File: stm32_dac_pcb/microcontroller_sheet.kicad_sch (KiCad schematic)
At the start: 2 parts, among them J201 Conn_01x03, U101 STM32F411CEUx

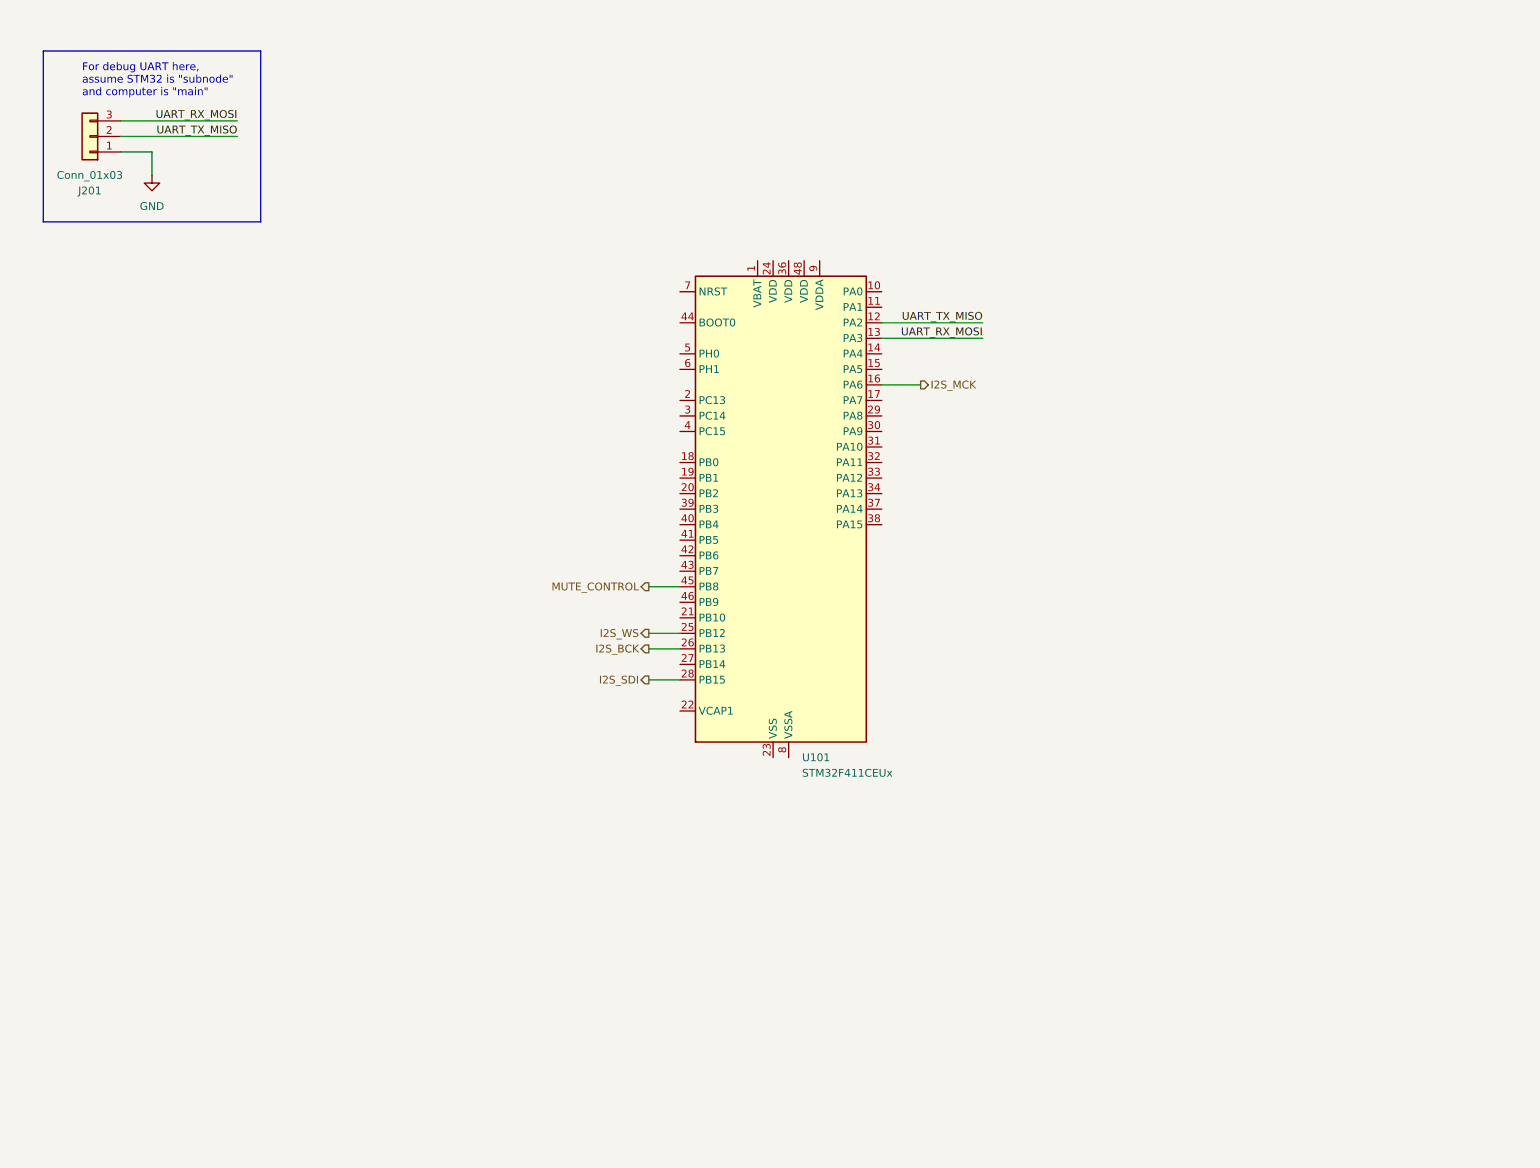
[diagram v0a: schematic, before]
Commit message: Add missing TODOs and USB plug
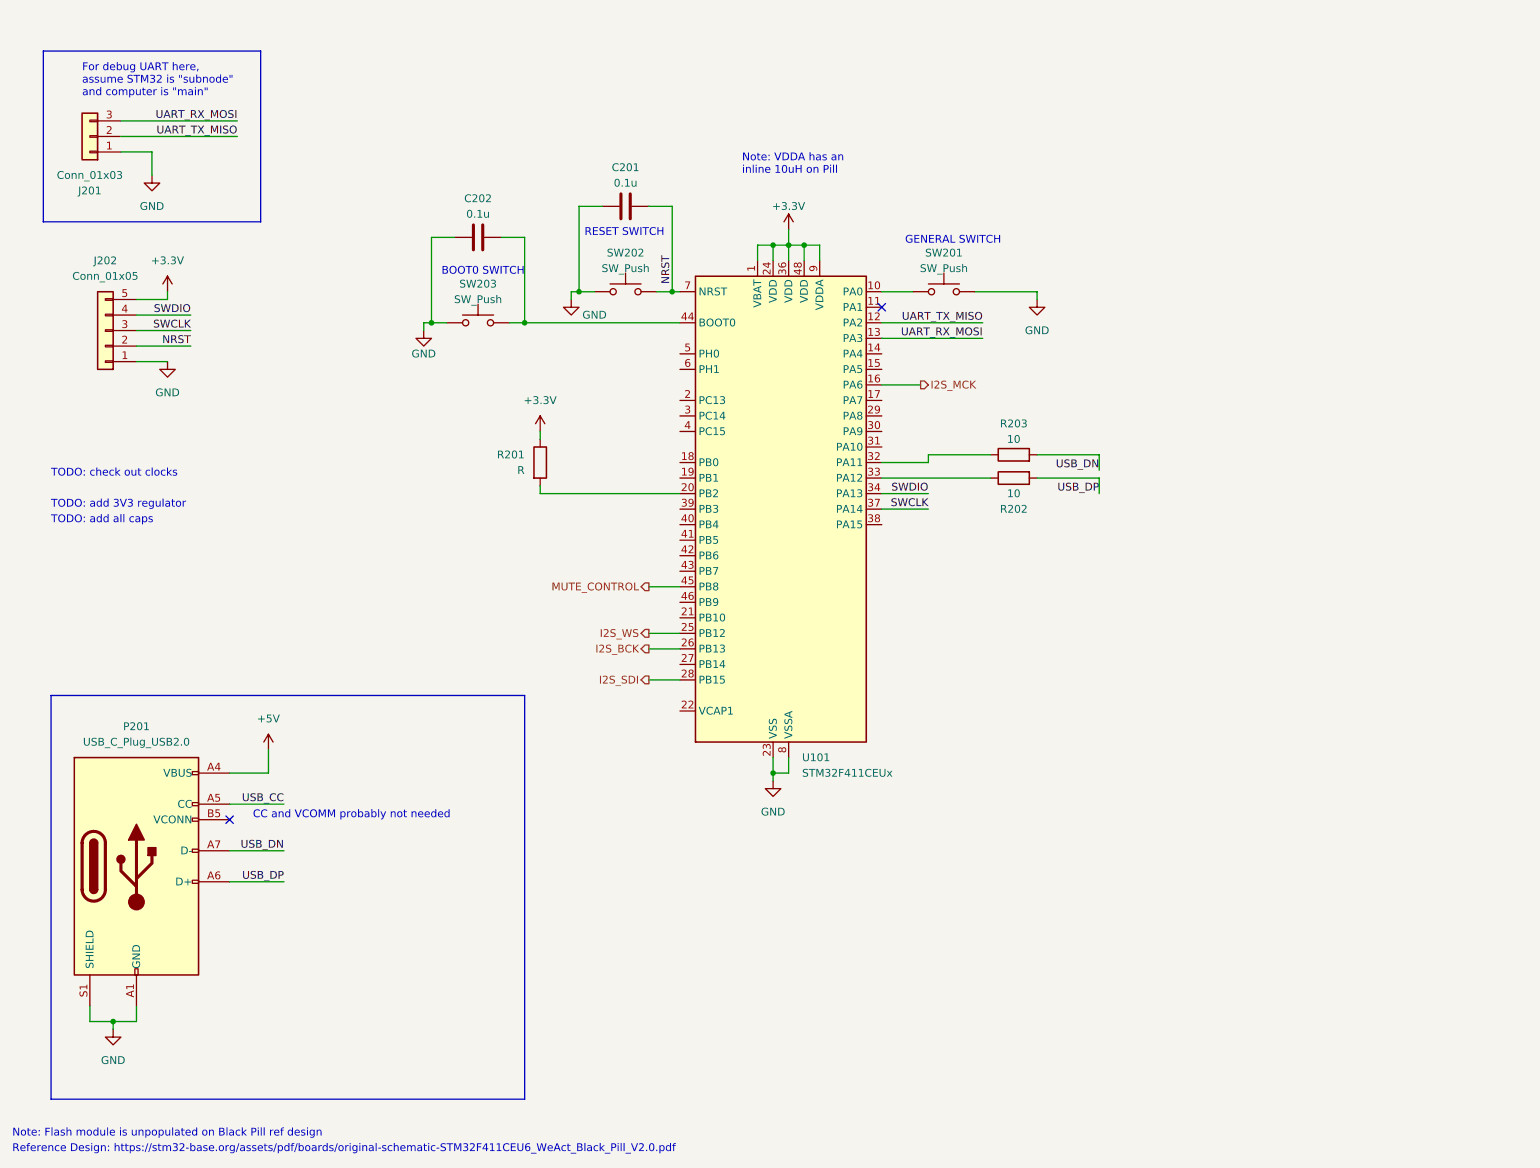
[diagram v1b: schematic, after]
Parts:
- added C201, C202: 0.1u, symbol Device:C
- added J202: Conn_01x05, symbol Connector_Generic:Conn_01x05
- added P201: USB_C_Plug_USB2.0, symbol Connector:USB_C_Plug_USB2.0
- added R201: R, symbol Device:R
- added R202, R203: 10, symbol Device:R
- added SW201, SW202, SW203: SW_Push, symbol Switch:SW_Push
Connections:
- net GND: now also U101.23 (VSS), U101.35 (VSS), U101.47 (VSS), U101.49 (VSS), U101.8 (VSSA), C201.1, C202.1, J202.1 (Pin_1), P201.A1 (GND), P201.A12 (GND), P201.B1 (GND), P201.B12 (GND), P201.S1 (SHIELD), SW201.2, SW202.2, SW203.2
- net +3.3V: now reaches U101.1 (VBAT)
- net +3.3V: now also U101.24 (VDD), U101.36 (VDD), U101.48 (VDD), U101.9 (VDDA), J202.5 (Pin_5), R201.1
- net at U101.10 (PA0): now also SW201.1
- net at U101.20 (PB2): now also R201.2
- net at U101.32 (PA11): now also R203.1
- net at U101.33 (PA12): now also R202.1
- net SWDIO: now reaches U101.34 (PA13)
- net SWDIO: now also J202.4 (Pin_4)
- net SWCLK: now reaches U101.37 (PA14)
- net SWCLK: now also J202.3 (Pin_3)
- net at U101.44 (BOOT0): now also C202.2, SW203.1
- net NRST: now reaches U101.7 (NRST)
- net NRST: now also C201.2, J202.2 (Pin_2), SW202.1
- new net +5V: P201.A4 (VBUS), P201.A9 (VBUS), P201.B4 (VBUS), P201.B9 (VBUS)
- new net USB_CC: P201.A5 (CC)
- new net USB_DN: P201.A7 (D-), R203.2
- new net USB_DP: P201.A6 (D+), R202.2
- no-connect marks 0 -> 2
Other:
- note added: "BOOT0 SWITCH"
- note added: "CC and VCOMM probably not needed"
- note added: "GENERAL SWITCH"
- note added: "Note: Flash module is unpopulated on Black Pill ref design"
- note added: "Note: VDDA has an inline 10uH on Pill"
- note added: "RESET SWITCH"
- note added: "Reference Design: https://stm32-base.org/assets/pdf/boards/original-schematic-STM32F411CEU6_WeAct_Black_Pill_V2.0.pdf"
- note added: "TODO: add 3V3 regulator"
- note added: "TODO: add all caps"
- note added: "TODO: check out clocks"

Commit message: Layout and routing
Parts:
- added C307 (x4): 0.1u, Capacitor_SMD:C_0603_1608Metric_Pad1.08x0.95mm_HandSolder, symbol Device:C
- C201, C202: footprint (none) -> Capacitor_SMD:C_0603_1608Metric_Pad1.08x0.95mm_HandSolder
- J201: footprint (none) -> Connector_PinHeader_2.00mm:PinHeader_1x03_P2.00mm_Vertical
- J202: footprint (none) -> Connector_PinHeader_2.00mm:PinHeader_1x05_P2.00mm_Vertical
- P201: footprint (none) -> Connector_USB:USB_C_Receptacle_CNCTech_C-ARA1-AK51X; LCSC (none) -> C2686966
- R201: value R -> 10k; footprint (none) -> Resistor_SMD:R_0603_1608Metric_Pad0.98x0.95mm_HandSolder
- R202, R203: footprint (none) -> Resistor_SMD:R_0603_1608Metric_Pad0.98x0.95mm_HandSolder
- SW201, SW202, SW203: footprint (none) -> 0_project_fp_lib:PushButtonSMD_2.93x3.9; LCSC (none) -> C18077675
- U101: LCSC (none) -> C60420
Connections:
- net +3.3V: now also C307.1, C307.1, C307.1, C307.1
- net GND: now also C307.2, C307.2, C307.2, C307.2
- net MIC_IN_2: now reaches U101.17 (PA7)
- net I2S_MCK renamed MIC_IN_1
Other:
- note added: "Decoupling for MCU"
- note added: "Note: I2S_MCLK used to be on PA6"
- note added: "Programming Header"
- note added: "TODO: LEDs"
- note added: "USB: LCSC C2686966 G-Switch GT-USB-7029DB"
- note removed: "TODO: add 3V3 regulator"
- note removed: "TODO: add all caps"

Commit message: Mostly finish up
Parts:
- added C307: 2.2u, Capacitor_SMD:C_0603_1608Metric_Pad1.08x0.95mm_HandSolder, symbol Device:C
- added J203: Conn_01x01, Connector_PinHeader_2.00mm:PinHeader_1x01_P2.00mm_Vertical, symbol Connector_Generic:Conn_01x01
- added R204: 5.1k, Resistor_SMD:R_0603_1608Metric_Pad0.98x0.95mm_HandSolder, symbol Device:R
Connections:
- net GND: now also C307.2, R204.2
- net at U101.22 (VCAP1): now also C307.1
- net at P201.B5 (VCONN): now also J203.1 (Pin_1)
- net USB_CC: no longer names the net of P201.A5 (CC)
- net USB_CC: now also R204.1
- no-connect marks 2 -> 22
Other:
- note added: "VCONN probably not needed"
- note removed: "CC and VCOMM probably not needed"
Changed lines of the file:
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@@
   (junction (at 220.98 33.02) (diameter 0) (color 0 0 0 0)
   )
-  (no_connect (at 49.53 147.32))
+  (no_connect (at 156.21 81.28))
+  (no_connect (at 123.19 101.6))
+  (no_connect (at 123.19 88.9))
+  (no_connect (at 123.19 106.68))
+  (no_connect (at 156.21 71.12))
+  (no_connect (at 123.19 99.06))
+  (no_connect (at 123.19 111.76))
+  (no_connect (at 123.19 83.82))
+  (no_connect (at 123.19 114.3))
+  (no_connect (at 123.19 73.66))
+  (no_connect (at 156.21 86.36))
+  (no_connect (at 123.19 78.74))
+  (no_connect (at 123.19 91.44))
+  (no_connect (at 156.21 73.66))
+  (no_connect (at 123.19 121.92))
+  (no_connect (at 156.21 99.06))
+  (no_connect (at 123.19 104.14))
   (no_connect (at 156.21 63.5))
+  (no_connect (at 156.21 83.82))
+  (no_connect (at 123.19 81.28))
+  (no_connect (at 123.19 96.52))
+  (no_connect (at 123.19 71.12))
   (wire (pts (xy 143.51 53.34) (xy 140.97 53.34))
     (stroke (width 0) (type default))
@@
     (stroke (width 0) (type default))
   )
+  (wire (pts (xy 49.53 147.32) (xy 63.5 147.32))
+    (stroke (width 0) (type default))
+  )
   (wire (pts (xy 171.45 60.96) (xy 181.61 60.96))
     (stroke (width 0) (type default))
   )
-  (wire (pts (xy 49.53 144.78) (xy 58.42 144.78))
+  (wire (pts (xy 49.53 144.78) (xy 68.58 144.78))
     (stroke (width 0) (type default))
   )
@@
     (stroke (width 0) (type default))
   )
+  (wire (pts (xy 119.38 139.7) (xy 119.38 142.24))
+    (stroke (width 0) (type default))
+  )
   (wire (pts (xy 121.92 60.96) (xy 123.19 60.96))
     (stroke (width 0) (type default))
@@
     (stroke (width 0) (type default))
   )
+  (wire (pts (xy 119.38 129.54) (xy 123.19 129.54))
+    (stroke (width 0) (type default))
+  )
   (wire (pts (xy 242.57 33.02) (xy 256.54 33.02))
     (stroke (width 0) (type default))
@@
     (stroke (width 0) (type default))
   )
+  (wire (pts (xy 63.5 147.32) (xy 63.5 166.37))
+    (stroke (width 0) (type default))
+  )
   (wire (pts (xy 156.21 96.52) (xy 163.83 96.52))
     (stroke (width 0) (type default))
@@
     (stroke (width 0) (type default))
   )
+  (wire (pts (xy 63.5 166.37) (xy 64.77 166.37))
+    (stroke (width 0) (type default))
+  )
   (wire (pts (xy 215.9 33.02) (xy 220.98 33.02))
     (stroke (width 0) (type default))
@@
     (stroke (width 0) (type default))
   )
+  (wire (pts (xy 119.38 132.08) (xy 119.38 129.54))
+    (stroke (width 0) (type default))
+  )
   (wire (pts (xy 156.21 76.2) (xy 162.56 76.2))
     (stroke (width 0) (type default))
@@
     (stroke (width 0) (type default))
   )
+  (wire (pts (xy 68.58 153.67) (xy 68.58 156.21))
+    (stroke (width 0) (type default))
+  )
   (wire (pts (xy 191.77 87.63) (xy 191.77 90.17))
+    (stroke (width 0) (type default))
+  )
+  (wire (pts (xy 68.58 146.05) (xy 68.58 144.78))
     (stroke (width 0) (type default))
   )
@@
     (effects (font (size 1.27 1.27)) (justify left bottom))
   )
-  (text "CC and VCOMM probably not needed" (at 53.34 147.32 0)
+  (text "VCONN probably not needed" (at 59.69 171.45 0)
     (effects (font (size 1.27 1.27)) (justify left bottom))
   )
@@
   )
   (label "SWCLK" (at 163.83 96.52 180) (fields_autoplaced)
-    (effects (font (size 1.27 1.27)) (justify right bottom))
-  )
-  (label "USB_CC" (at 58.42 144.78 180) (fields_autoplaced)
     (effects (font (size 1.27 1.27)) (justify right bottom))
   )
@@
     )
   )
+  (symbol (lib_id "power:GND") (at 119.38 142.24 0) (unit 1)
+    (in_bom yes) (on_board yes) (dnp no)
+    (property "Reference" "#PWR0214" (at 119.38 148.59 0)
+      (effects (font (size 1.27 1.27)) hide)
+    )
+    (property "Value" "GND" (at 119.38 146.05 0)
+      (effects (font (size 1.27 1.27)))
+    )
+    (property "Footprint" "" (at 119.38 142.24 0)
+      (effects (font (size 1.27 1.27)) hide)
+    )
+    (property "Datasheet" "" (at 119.38 142.24 0)
+      (effects (font (size 1.27 1.27)) hide)
+    )
+    (pin "1")
+    (instances
+      (project "stm32_dac_pcb"
+        (path "/c2a919d7-4260-41a9-9bc5-9737c1b4d769/b77d31d3-d267-4ae4-806f-e210a5dd1f2c"
+          (reference "#PWR0214") (unit 1)
+        )
+      )
+    )
+  )
+  (symbol (lib_id "power:GND") (at 68.58 156.21 0) (unit 1)
+    (in_bom yes) (on_board yes) (dnp no)
+    (property "Reference" "#PWR0215" (at 68.58 162.56 0)
+      (effects (font (size 1.27 1.27)) hide)
+    )
+    (property "Value" "GND" (at 68.58 160.02 0)
+      (effects (font (size 1.27 1.27)))
+    )
+    (property "Footprint" "" (at 68.58 156.21 0)
+      (effects (font (size 1.27 1.27)) hide)
+    )
+    (property "Datasheet" "" (at 68.58 156.21 0)
+      (effects (font (size 1.27 1.27)) hide)
+    )
+    (pin "1")
+    (instances
+      (project "stm32_dac_pcb"
+        (path "/c2a919d7-4260-41a9-9bc5-9737c1b4d769/b77d31d3-d267-4ae4-806f-e210a5dd1f2c"
+          (reference "#PWR0215") (unit 1)
+        )
+      )
+    )
+  )
   (symbol (lib_id "Device:C") (at 114.3 46.99 90) (unit 1)
     (in_bom yes) (on_board yes) (dnp no)
@@
         (path "/c2a919d7-4260-41a9-9bc5-9737c1b4d769/b77d31d3-d267-4ae4-806f-e210a5dd1f2c"
           (reference "#PWR0201") (unit 1)
+        )
+      )
+    )
+  )
+  (symbol (lib_id "Device:C") (at 119.38 135.89 0) (mirror y) (unit 1)
+    (in_bom yes) (on_board yes) (dnp no)
+    (property "Reference" "C307" (at 116.84 134.62 0)
+      (effects (font (size 1.27 1.27)) (justify left))
+    )
+    (property "Value" "2.2u" (at 116.84 137.16 0)
+      (effects (font (size 1.27 1.27)) (justify left))
+    )
+    (property "Footprint" "Capacitor_SMD:C_0603_1608Metric_Pad1.08x0.95mm_HandSolder" (at 118.4148 139.7 0)
+      (effects (font (size 1.27 1.27)) hide)
+    )
+    (property "Datasheet" "~" (at 119.38 135.89 0)
+      (effects (font (size 1.27 1.27)) hide)
+    )
+    (pin "1")
+    (pin "2")
+    (instances
+      (project "stm32_dac_pcb"
+        (path "/c2a919d7-4260-41a9-9bc5-9737c1b4d769/0d9874eb-1d6a-4e96-92eb-7b248f8c9096"
+          (reference "C307") (unit 1)
+        )
+        (path "/c2a919d7-4260-41a9-9bc5-9737c1b4d769/b77d31d3-d267-4ae4-806f-e210a5dd1f2c"
+          (reference "C207") (unit 1)
+        )
+      )
+    )
+  )
+  (symbol (lib_id "Connector_Generic:Conn_01x01") (at 69.85 166.37 0) (unit 1)
+    (in_bom yes) (on_board yes) (dnp no) (fields_autoplaced)
+    (property "Reference" "J203" (at 72.39 165.1 0)
+      (effects (font (size 1.27 1.27)) (justify left))
+    )
+    (property "Value" "Conn_01x01" (at 72.39 167.64 0)
+      (effects (font (size 1.27 1.27)) (justify left))
+    )
+    (property "Footprint" "Connector_PinHeader_2.00mm:PinHeader_1x01_P2.00mm_Vertical" (at 69.85 166.37 0)
+      (effects (font (size 1.27 1.27)) hide)
+    )
+    (property "Datasheet" "~" (at 69.85 166.37 0)
+      (effects (font (size 1.27 1.27)) hide)
+    )
+    (pin "1")
+    (instances
+      (project "stm32_dac_pcb"
+        (path "/c2a919d7-4260-41a9-9bc5-9737c1b4d769/b77d31d3-d267-4ae4-806f-e210a5dd1f2c"
+          (reference "J203") (unit 1)
         )
       )
@@
         )
       )
+    )
+  )
+  (symbol (lib_id "Device:R") (at 68.58 149.86 0) (mirror y) (unit 1)
+    (in_bom yes) (on_board yes) (dnp no)
+    (property "Reference" "R204" (at 71.12 148.59 0)
+      (effects (font (size 1.27 1.27)) (justify right))
+    )
+    (property "Value" "5.1k" (at 71.12 151.13 0)
+      (effects (font (size 1.27 1.27)) (justify right))
+    )
+    (property "Footprint" "Resistor_SMD:R_0603_1608Metric_Pad0.98x0.95mm_HandSolder" (at 70.358 149.86 90)
+      (effects (font (size 1.27 1.27)) hide)
+    )
+    (property "Datasheet" "~" (at 68.58 149.86 0)
+      (effects (font (size 1.27 1.27)) hide)
+    )
+    (pin "2")
+    (pin "1")
+    (instances
+      (project "stm32_dac_pcb"
+        (path "/c2a919d7-4260-41a9-9bc5-9737c1b4d769/b77d31d3-d267-4ae4-806f-e210a5dd1f2c"
+          (reference "R204") (unit 1)
+        )
+      )
